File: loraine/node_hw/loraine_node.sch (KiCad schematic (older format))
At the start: 39 parts, among them CON1 BARREL_JACK, IC1 ATTINY2313A-S, P1 MOLEX, P2 MOLEX, P3 SOLDER_PAD, P4 ICSP, P5 OUTPUTS, P6 BUS, Q1 BD679, Q2 BD679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

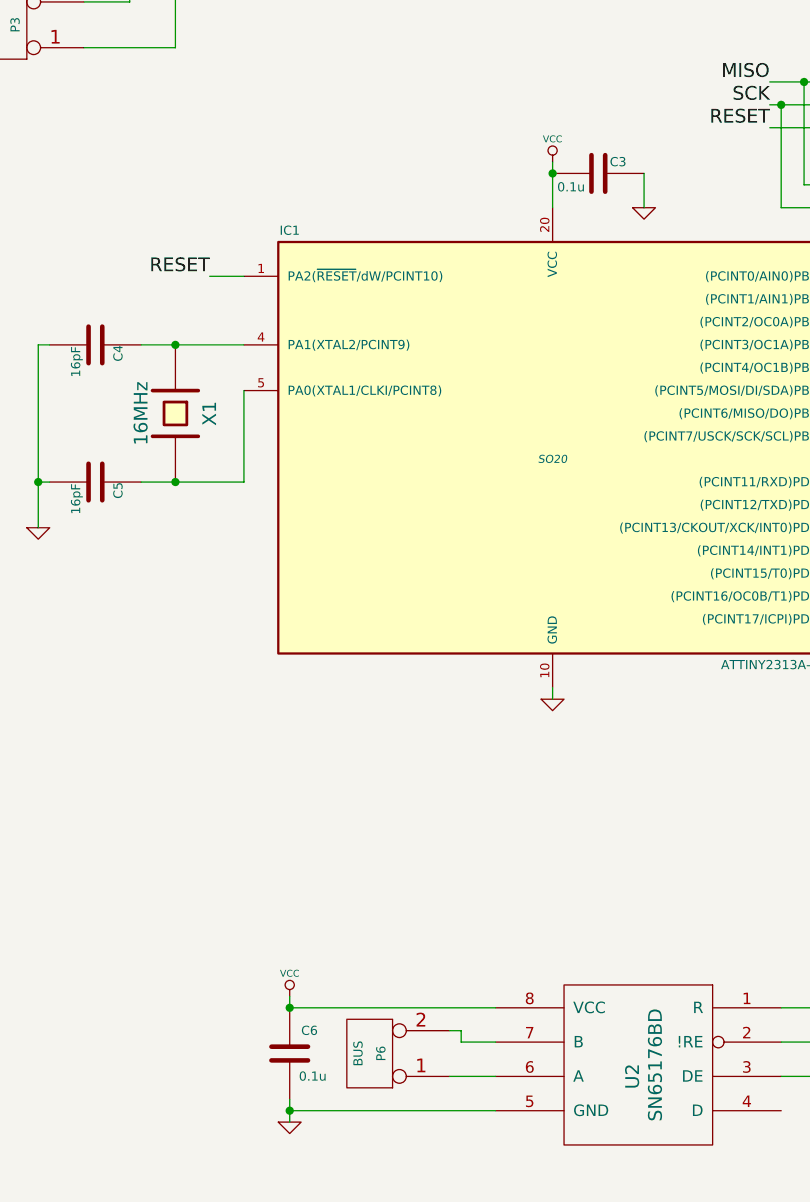
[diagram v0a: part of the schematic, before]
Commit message: Added bus thu connector
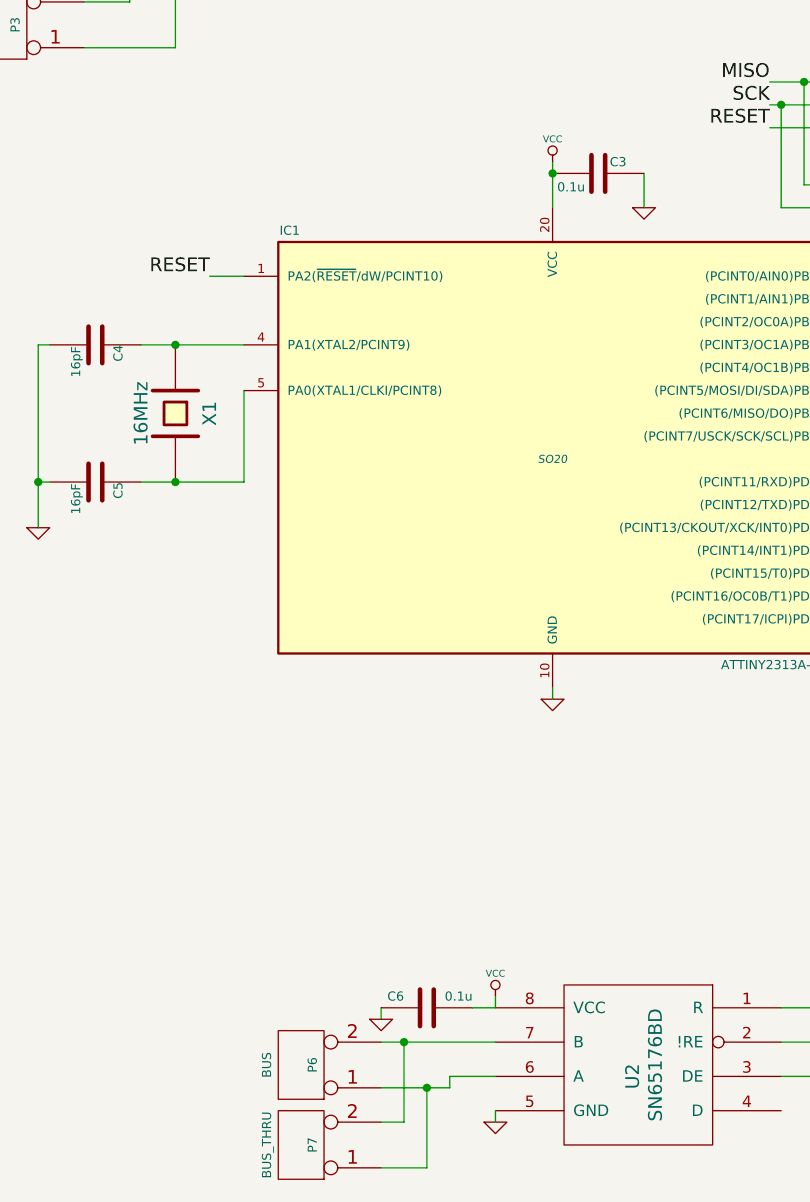
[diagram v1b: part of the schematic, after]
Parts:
- added P7: BUS_THRU, symbol CONN_2
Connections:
- net GND: now also C6.1; no longer C6.2
- net VCC: now also C6.2; no longer C6.1
- net at P6.1 (P1), U2.6 (A): now also P7.1 (P1)
- net at P6.2 (PM), U2.7 (B): now also P7.2 (PM)
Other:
- moved on the sheet: C6, P6
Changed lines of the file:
@@
 	4750 7000 4750 7250
 $Comp
-L GND #PWR14
+L GND #PWR15
 U 1 1 53388FDD
 P 4750 7250
-F 0 "#PWR14" H 4750 7250 30  0001 C CNN
+F 0 "#PWR15" H 4750 7250 30  0001 C CNN
 F 1 "GND" H 4750 7180 30  0001 C CNN
 F 2 "" H 4750 7250 60  0000 C CNN
@@
 L CONN_2 P6
 U 1 1 5338950E
-P 2650 7050
-F 0 "P6" V 2600 7050 40  0000 C CNN
-F 1 "BUS" V 2700 7050 40  0000 C CNN
-F 2 "" H 2650 7050 60  0000 C CNN
-F 3 "" H 2650 7050 60  0000 C CNN
-	1    2650 7050
+P 2350 7100
+F 0 "P6" V 2300 7100 40  0000 C CNN
+F 1 "BUS" V 2500 7100 40  0000 C CNN
+F 2 "" H 2350 7100 60  0000 C CNN
+F 3 "" H 2350 7100 60  0000 C CNN
+	1    2350 7100
 	-1   0    0    1
 $EndComp
-Wire Wire Line
-	3000 7150 3200 7150
 Wire Wire Line
 	6900 5100 7350 5100
@@
 L C C6
 U 1 1 5338A896
-P 2300 7050
-F 0 "C6" H 2350 7150 40  0000 L CNN
-F 1 "0.1u" H 2340 6950 40  0000 L CNN
-F 2 "" H 2338 6900 30  0000 C CNN
-F 3 "" H 2300 7050 60  0000 C CNN
-	1    2300 7050
-	1    0    0    -1
-$EndComp
-Wire Wire Line
-	3000 6950 3050 6950
-Wire Wire Line
-	3050 6950 3050 7000
-Wire Wire Line
-	3050 7000 3200 7000
-Connection ~ 2300 6850
-Wire Wire Line
-	2300 7250 2300 7350
-Connection ~ 2300 7300
+P 2900 6850
+F 0 "C6" V 2950 6950 40  0000 L CNN
+F 1 "0.1u" V 2950 6650 40  0000 L CNN
+F 2 "" H 2938 6700 30  0000 C CNN
+F 3 "" H 2900 6850 60  0000 C CNN
+	1    2900 6850
+	0    -1   -1   0
+$EndComp
+Wire Wire Line
+	2700 7000 3200 7000
 $Comp
 L C C3
@@
 	5700 3000 5700 3050
 $Comp
-L GND #PWR15
+L GND #PWR16
 U 1 1 5338FCA4
-P 2300 7350
-F 0 "#PWR15" H 2300 7350 30  0001 C CNN
-F 1 "GND" H 2300 7280 30  0001 C CNN
-F 2 "" H 2300 7350 60  0000 C CNN
-F 3 "" H 2300 7350 60  0000 C CNN
-	1    2300 7350
-	1    0    0    -1
-$EndComp
-Wire Wire Line
-	3200 7300 2300 7300
+P 3200 7350
+F 0 "#PWR16" H 3200 7350 30  0001 C CNN
+F 1 "GND" H 3200 7280 30  0001 C CNN
+F 2 "" H 3200 7350 60  0000 C CNN
+F 3 "" H 3200 7350 60  0000 C CNN
+	1    3200 7350
+	1    0    0    -1
+$EndComp
+Wire Wire Line
+	3200 7300 3200 7300
 $Comp
 L +12V #PWR2
@@
 	2200 1100 2200 1150
 Wire Wire Line
-	3450 3350 3450 3150
+	3450 3150 3450 3350
 $Comp
 L VCC #PWR7
@@
 L VCC #PWR13
 U 1 1 5339091E
-P 2300 6800
-F 0 "#PWR13" H 2300 6900 30  0001 C CNN
-F 1 "VCC" H 2300 6900 30  0000 C CNN
-F 2 "" H 2300 6800 60  0000 C CNN
-F 3 "" H 2300 6800 60  0000 C CNN
-	1    2300 6800
-	1    0    0    -1
-$EndComp
-Wire Wire Line
-	2300 6850 2300 6800
-Wire Wire Line
-	2300 6850 3200 6850
+P 3200 6800
+F 0 "#PWR13" H 3200 6900 30  0001 C CNN
+F 1 "VCC" H 3200 6900 30  0000 C CNN
+F 2 "" H 3200 6800 60  0000 C CNN
+F 3 "" H 3200 6800 60  0000 C CNN
+	1    3200 6800
+	1    0    0    -1
+$EndComp
+Wire Wire Line
+	3200 6850 3200 6800
 $Comp
 L +12V #PWR10
@@
 Wire Wire Line
 	6150 2300 6500 2300
+Wire Wire Line
+	3200 7300 3200 7350
+Wire Wire Line
+	3100 6850 3200 6850
+$Comp
+L GND #PWR14
+U 1 1 5339D1EB
+P 2700 6900
+F 0 "#PWR14" H 2700 6900 30  0001 C CNN
+F 1 "GND" H 2700 6830 30  0001 C CNN
+F 2 "" H 2700 6900 60  0000 C CNN
+F 3 "" H 2700 6900 60  0000 C CNN
+	1    2700 6900
+	1    0    0    -1
+$EndComp
+Wire Wire Line
+	2700 6850 2700 6900
+Wire Wire Line
+	2700 7200 3000 7200
+Wire Wire Line
+	3000 7200 3000 7150
+Wire Wire Line
+	3000 7150 3200 7150
+$Comp
+L CONN_2 P7
+U 1 1 5339D3B6
+P 2350 7450
+F 0 "P7" V 2300 7450 40  0000 C CNN
+F 1 "BUS_THRU" V 2500 7450 40  0000 C CNN
+F 2 "" H 2350 7450 60  0000 C CNN
+F 3 "" H 2350 7450 60  0000 C CNN
+	1    2350 7450
+	-1   0    0    1
+$EndComp
+Wire Wire Line
+	2800 7000 2800 7350
+Wire Wire Line
+	2800 7350 2700 7350
+Connection ~ 2800 7000
+Wire Wire Line
+	2900 7200 2900 7550
+Wire Wire Line
+	2900 7550 2700 7550
+Connection ~ 2900 7200
 $EndSCHEMATC

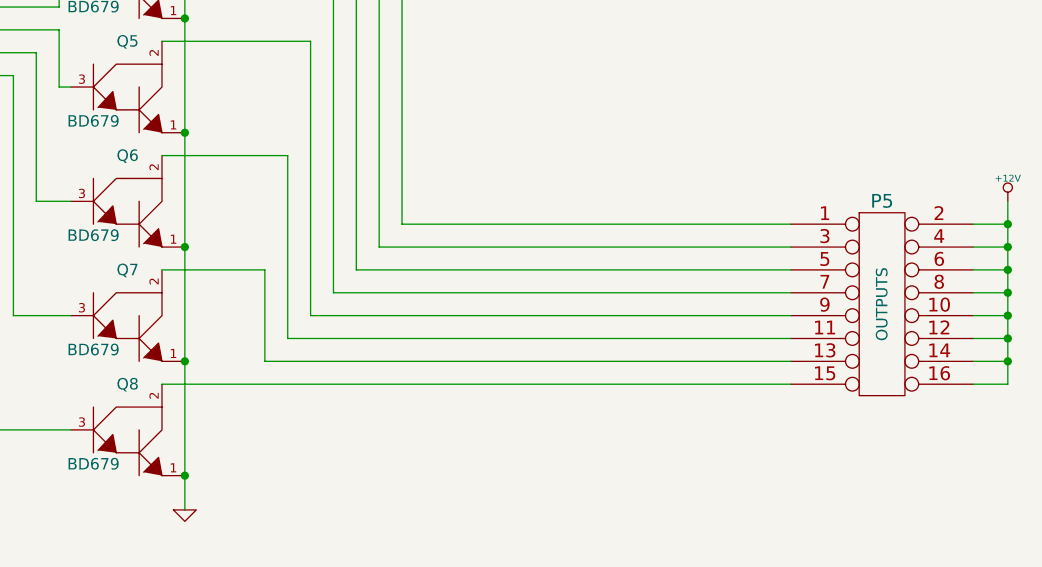
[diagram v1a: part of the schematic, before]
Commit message: PCB rev2
Routed PTH darlingtons
swapped order of output pinout to make pcb route better
'L'-shaped PCB for adam ;)
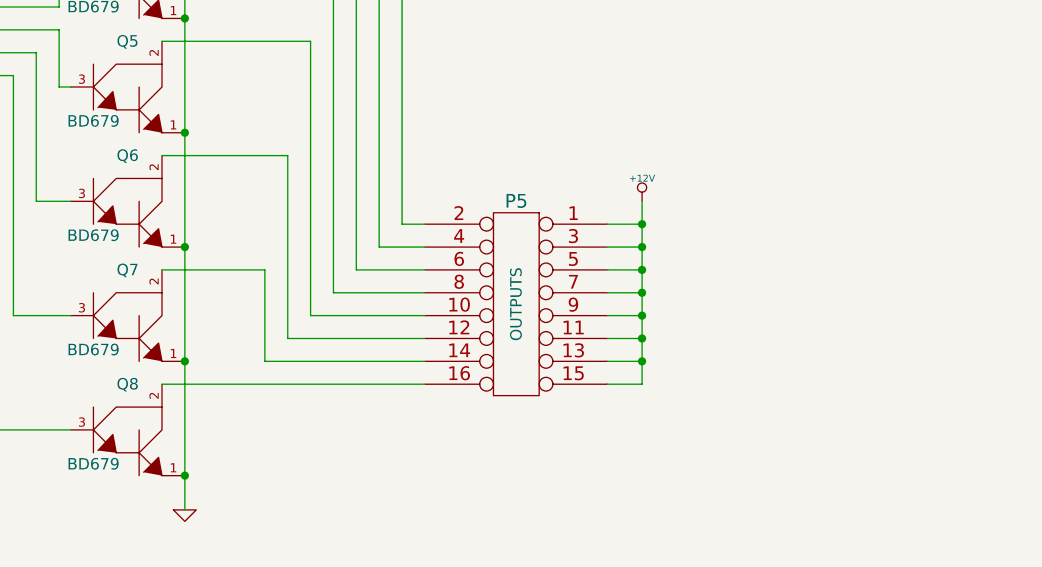
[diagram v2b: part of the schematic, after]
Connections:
- net +12V: now also P5.1, P5.11, P5.13, P5.15, P5.3, P5.5, P5.7, P5.9; no longer P5.10, P5.12, P5.14, P5.16, P5.2, P5.4, P5.6, P5.8
- net at D1.2 (K), Q1.2: now also P5.2; no longer P5.1
- net at D2.2 (K), Q2.2: now also P5.4; no longer P5.3
- net at D3.2 (K), Q3.2: now also P5.6; no longer P5.5
- net at Q6.2: now also P5.12; no longer P5.11
- net at Q7.2: now also P5.14; no longer P5.13
- net at Q8.2: now also P5.16; no longer P5.15
- net at Q4.2: now also P5.8; no longer P5.7
- net at Q5.2: now also P5.10; no longer P5.9
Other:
- moved on the sheet: P5

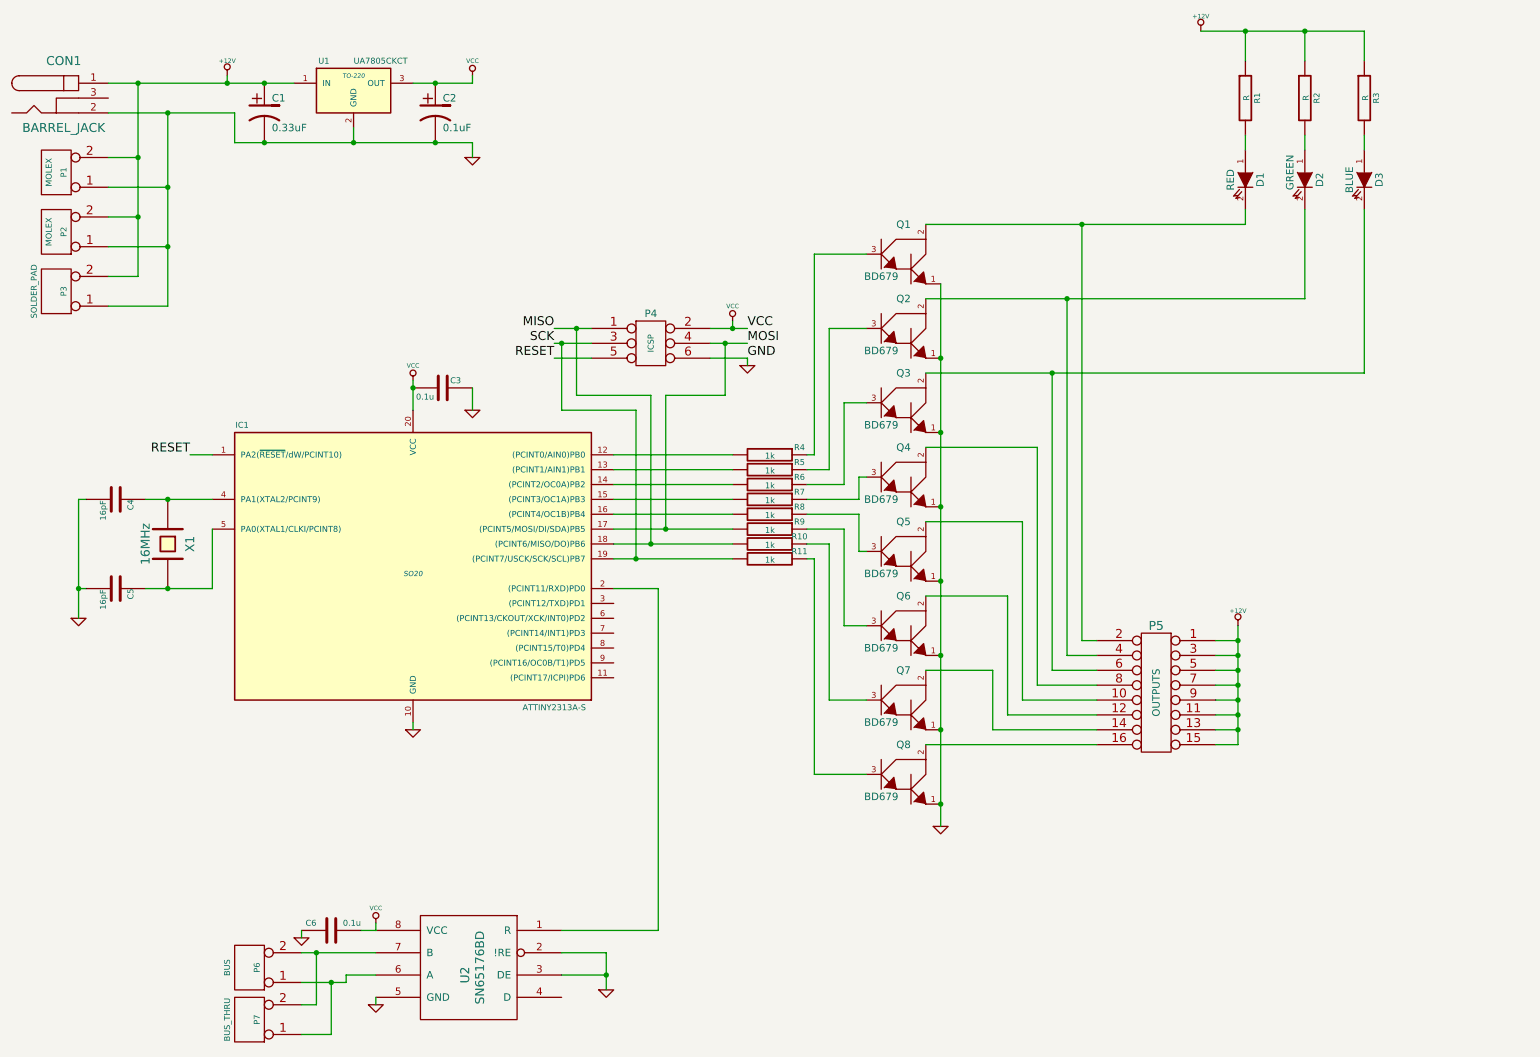
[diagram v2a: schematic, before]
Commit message: Added TL4242 driver ICs with support circuitry
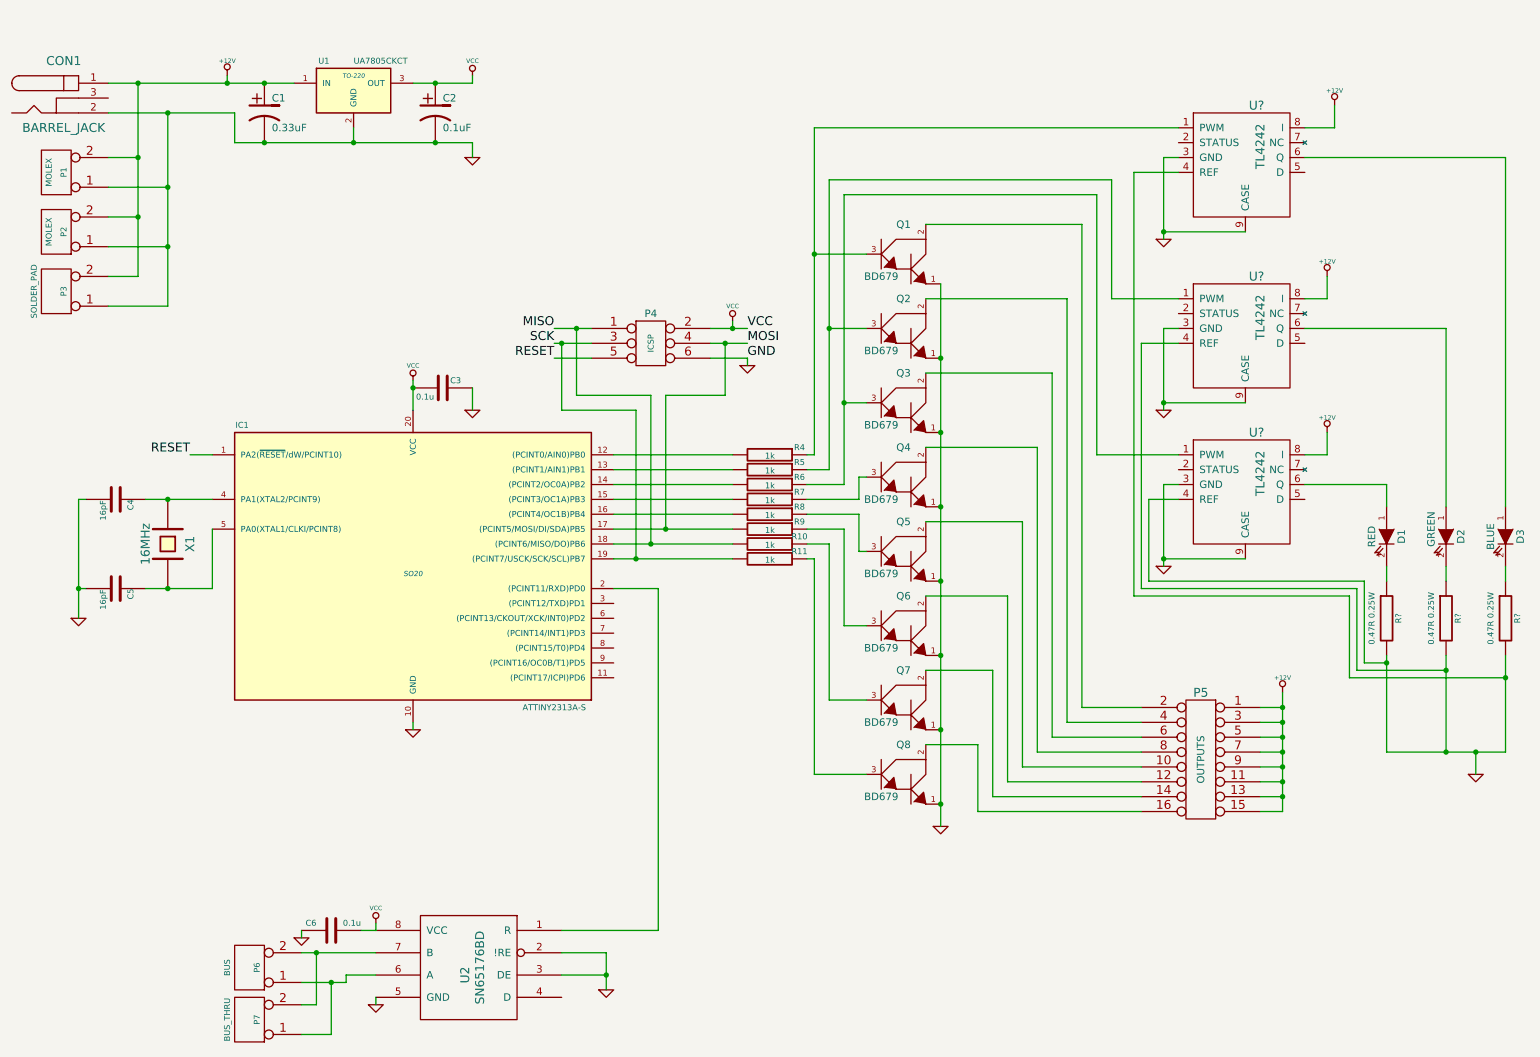
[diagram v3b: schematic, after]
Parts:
- removed R1, R2, R3: R, symbol R
- added R? (x3): 0.47R 0.25W, symbol R
- added U? (x3): TL4242, symbol TL4242
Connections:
- net +12V: now also U?.8 (I), U?.8 (I), U?.8 (I)
- net GND: now also R?.2, R?.2, R?.2, U?.3 (GND), U?.3 (GND), U?.3 (GND), U?.4 (REF), U?.4 (REF), U?.4 (REF), U?.9 (CASE), U?.9 (CASE), U?.9 (CASE)
- net at Q1.3, R4.1: now also U?.1 (PWM)
- net at Q2.3, R5.1: now also U?.1 (PWM)
- net at Q3.3, R6.1: now also U?.1 (PWM)
- net at D1.1 (A): now also U?.6 (Q)
- net at P5.2, Q1.2: no longer D1.2 (K)
- net at D2.1 (A): now also U?.6 (Q)
- net at P5.4, Q2.2: no longer D2.2 (K)
- net at D3.1 (A): now also U?.6 (Q)
- net at P5.6, Q3.2: no longer D3.2 (K)
- new net: D1.2 (K), R?.1
- new net: D2.2 (K), R?.1
- new net: D3.2 (K), R?.1
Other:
- moved on the sheet: D1, D2, D3, P5
